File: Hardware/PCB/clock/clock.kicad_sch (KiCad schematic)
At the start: 58 parts, among them J1 AudioJack2, J2 Synth_power_2x5, J3 AudioJack2, J4 AudioJack2, J5 AudioJack2, J6 AudioJack2, J7 AudioJack2, J8 Conn_02x04_Odd_Even, J9 Conn_02x04_Odd_Even, Q1 2N3904, SW1 RotaryEncoder, SW2 SW_Push, U1 40106

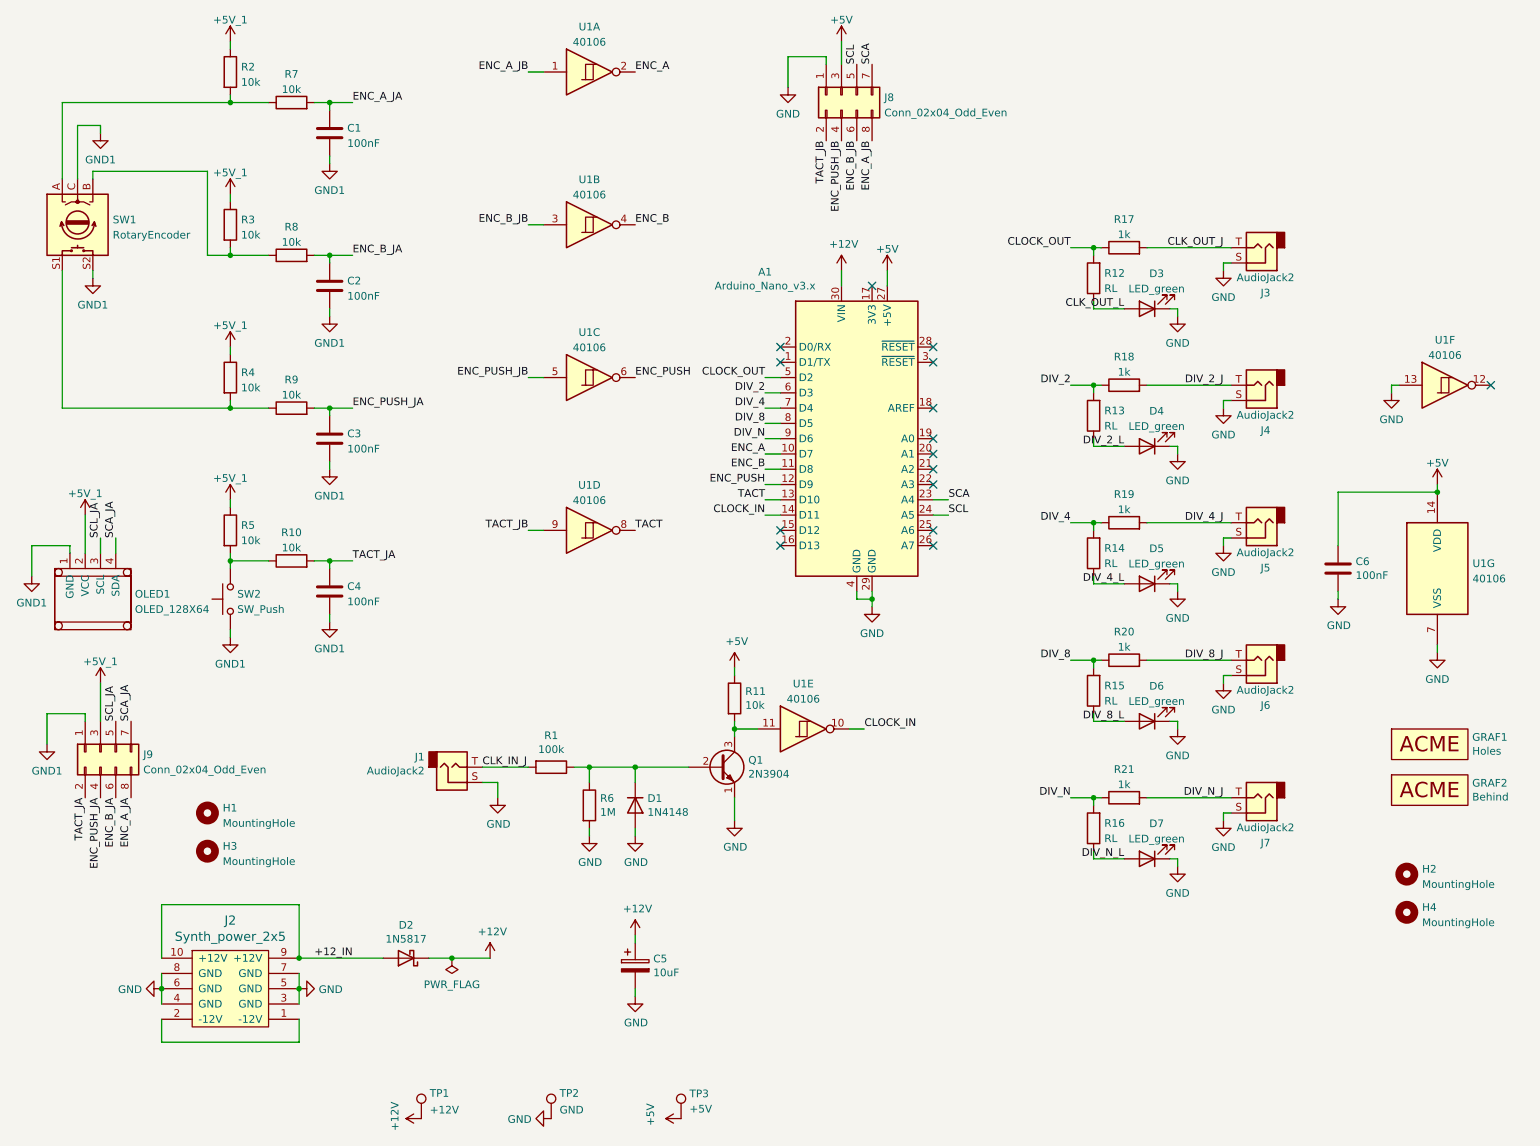
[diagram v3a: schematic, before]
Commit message: Add Zeners, reallocate XORs
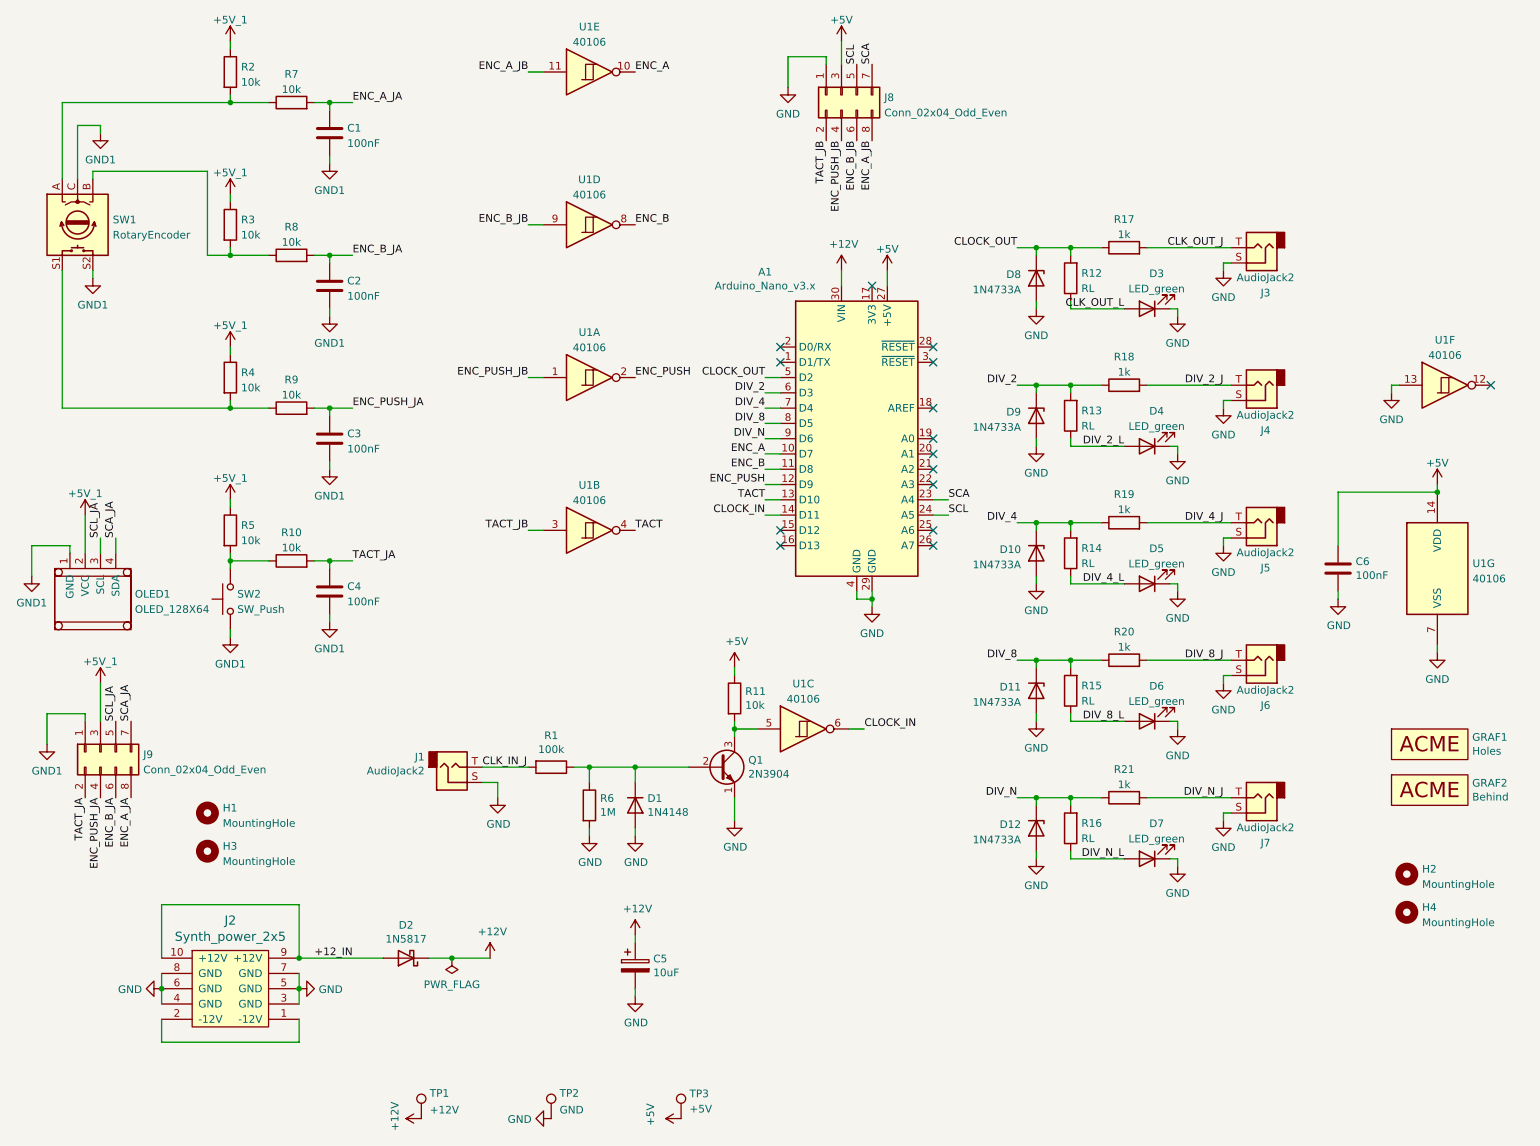
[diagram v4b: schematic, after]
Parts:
- added D10, D11, D12, D8, D9: 1N4733A, ao_tht:D_DO-41_SOD81_P10.16mm_Horizontal, symbol ao_symbols:1N4733A
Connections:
- net CLOCK_IN: now also U1.6; no longer U1.10
- net CLOCK_OUT: now also D8.1 (K)
- net DIV_2: now also D9.1 (K)
- net DIV_4: now also D10.1 (K)
- net DIV_8: now also D11.1 (K)
- net DIV_N: now also D12.1 (K)
- net ENC_A: now also U1.10; no longer U1.2
- net ENC_A_JB: now also U1.11; no longer U1.1
- net ENC_B: now also U1.8; no longer U1.4
- net ENC_B_JB: now also U1.9; no longer U1.3
- net ENC_PUSH: now also U1.2; no longer U1.6
- net ENC_PUSH_JB: now also U1.1; no longer U1.5
- net GND: now also D10.2 (A), D11.2 (A), D12.2 (A), D8.2 (A), D9.2 (A)
- net TACT: now also U1.4; no longer U1.8
- net TACT_JB: now also U1.3; no longer U1.9
- net at Q1.3 (C), R11.2: now also U1.5; no longer U1.11
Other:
- moved on the sheet: R12, R13, R14, R15, R16, U1A, U1B, U1C, U1D, U1E

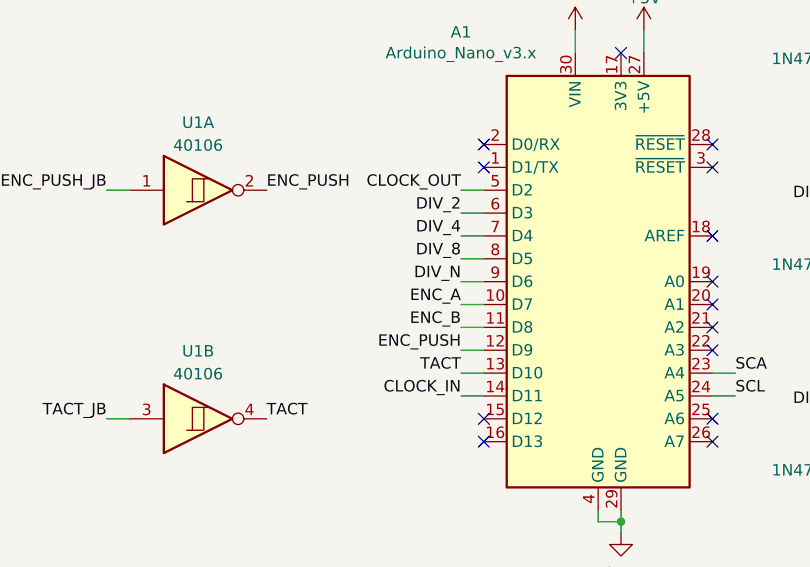
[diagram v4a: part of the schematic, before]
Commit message: Rearrange digital pins (for encoder to interrupt pin 2)
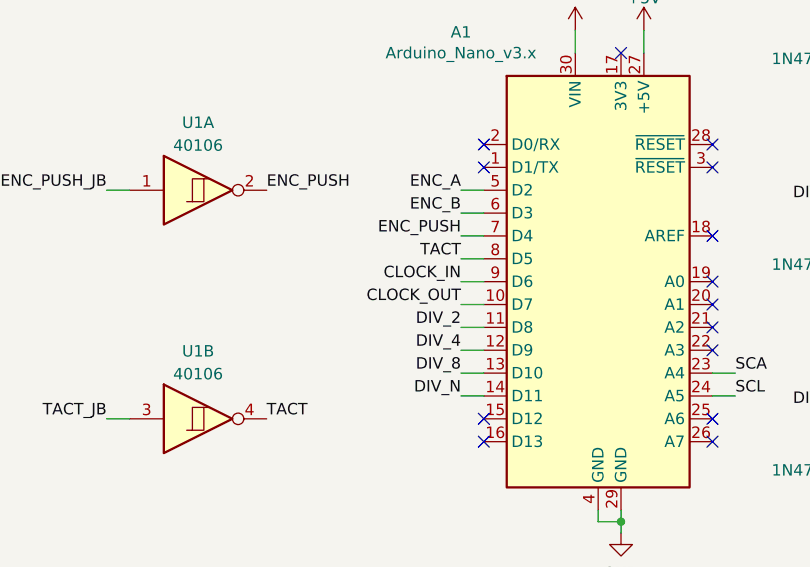
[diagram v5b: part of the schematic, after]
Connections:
- net CLOCK_IN: now also A1.9 (D6); no longer A1.14 (D11)
- net CLOCK_OUT: now also A1.10 (D7); no longer A1.5 (D2)
- net DIV_2: now also A1.11 (D8); no longer A1.6 (D3)
- net DIV_4: now also A1.12 (D9); no longer A1.7 (D4)
- net DIV_8: now also A1.13 (D10); no longer A1.8 (D5)
- net DIV_N: now also A1.14 (D11); no longer A1.9 (D6)
- net ENC_A: now also A1.5 (D2); no longer A1.10 (D7)
- net ENC_B: now also A1.6 (D3); no longer A1.11 (D8)
- net ENC_PUSH: now also A1.7 (D4); no longer A1.12 (D9)
- net TACT: now also A1.8 (D5); no longer A1.13 (D10)
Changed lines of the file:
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@@
     )
   )
-  (label "ENC_A" (at 139.7 88.9 180)
+  (label "ENC_A" (at 139.7 76.2 180)
     (effects (font (size 1.27 1.27)) (justify right bottom))
   )
@@
     (effects (font (size 1.27 1.27)) (justify left bottom))
   )
-  (label "DIV_N" (at 139.7 86.36 180)
+  (label "DIV_N" (at 139.7 99.06 180)
     (effects (font (size 1.27 1.27)) (justify right bottom))
   )
@@
     (effects (font (size 1.27 1.27)) (justify right bottom))
   )
-  (label "CLOCK_OUT" (at 139.7 76.2 180)
+  (label "CLOCK_OUT" (at 139.7 88.9 180)
     (effects (font (size 1.27 1.27)) (justify right bottom))
   )
@@
     (effects (font (size 1.27 1.27)) (justify left bottom))
   )
-  (label "DIV_2" (at 139.7 78.74 180)
+  (label "DIV_2" (at 139.7 91.44 180)
     (effects (font (size 1.27 1.27)) (justify right bottom))
   )
@@
     (effects (font (size 1.27 1.27)) (justify right bottom))
   )
-  (label "TACT" (at 139.7 96.52 180)
+  (label "TACT" (at 139.7 83.82 180)
     (effects (font (size 1.27 1.27)) (justify right bottom))
   )
@@
     (effects (font (size 1.27 1.27)) (justify left bottom))
   )
-  (label "CLOCK_IN" (at 139.7 99.06 180)
+  (label "CLOCK_IN" (at 139.7 86.36 180)
     (effects (font (size 1.27 1.27)) (justify right bottom))
   )
@@
     (effects (font (size 1.27 1.27)) (justify right bottom))
   )
-  (label "ENC_B" (at 139.7 91.44 180)
+  (label "ENC_B" (at 139.7 78.74 180)
     (effects (font (size 1.27 1.27)) (justify right bottom))
   )
-  (label "ENC_PUSH" (at 139.7 93.98 180)
+  (label "ENC_PUSH" (at 139.7 81.28 180)
     (effects (font (size 1.27 1.27)) (justify right bottom))
   )
@@
     (effects (font (size 1.27 1.27)) (justify right bottom))
   )
-  (label "DIV_4" (at 139.7 81.28 180)
+  (label "DIV_4" (at 139.7 93.98 180)
     (effects (font (size 1.27 1.27)) (justify right bottom))
   )
@@
     (effects (font (size 1.27 1.27)) (justify right bottom))
   )
-  (label "DIV_8" (at 139.7 83.82 180)
+  (label "DIV_8" (at 139.7 96.52 180)
     (effects (font (size 1.27 1.27)) (justify right bottom))
   )

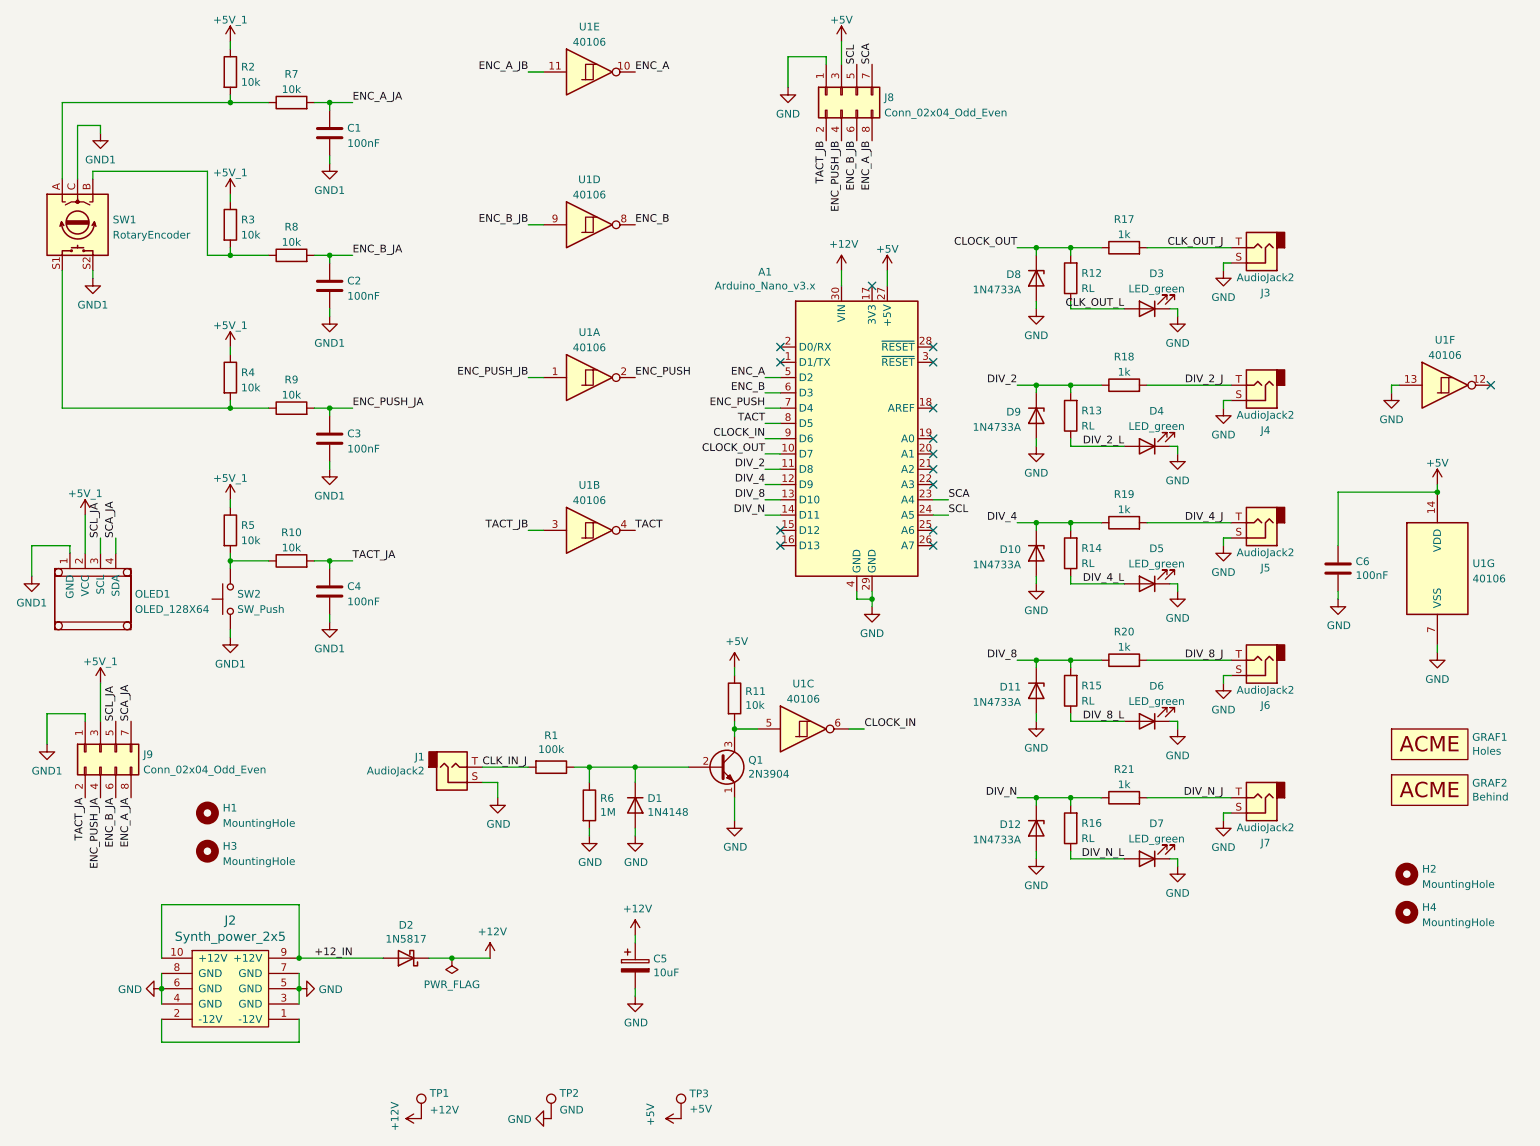
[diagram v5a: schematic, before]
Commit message: rm external clock, add beat output
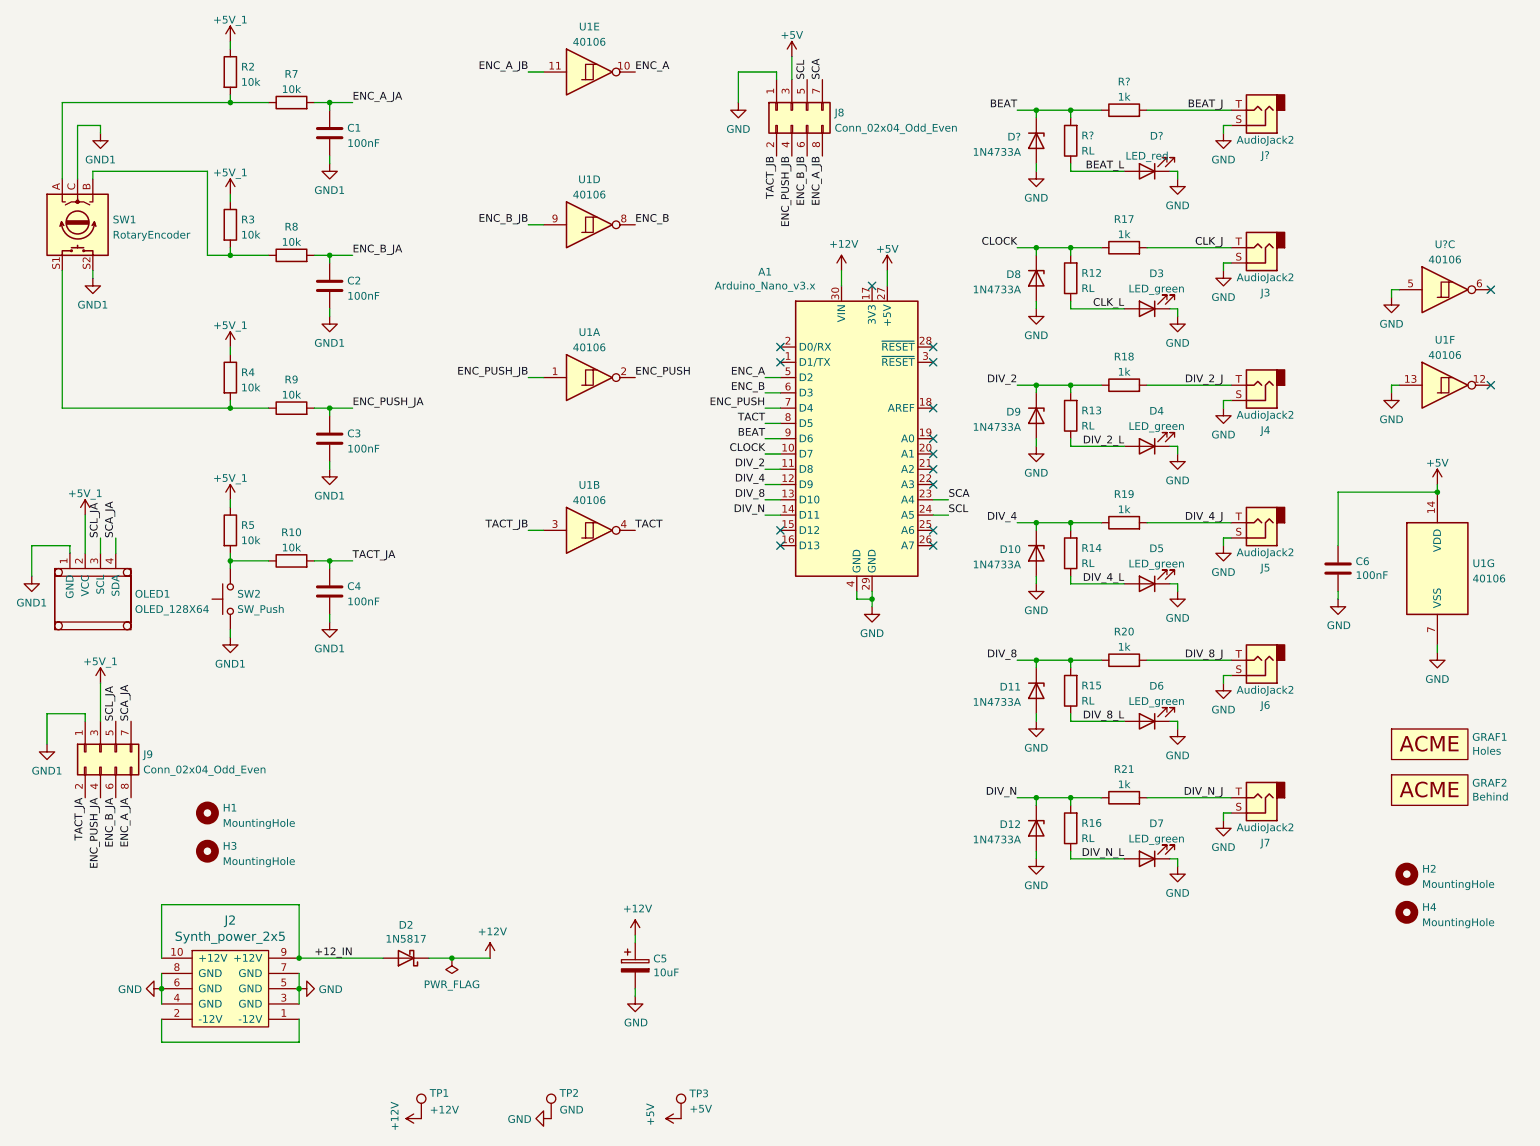
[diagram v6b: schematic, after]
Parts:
- removed D1: 1N4148, ao_tht:D_DO-35_SOD27_P7.62mm_Horizontal, symbol ao_symbols:1N4148
- removed J1: AudioJack2, ao_tht:Jack_6.35mm_PJ_629HAN_slots, symbol ao_symbols:AudioJack2
- removed Q1: 2N3904, ao_tht:TO-92_Inline_Wide, symbol ao_symbols:2N3904
- removed R1: 100k, ao_tht:R_Axial_DIN0204_L3.6mm_D1.6mm_P7.62mm_Horizontal, symbol ao_symbols:R
- removed R11: 10k, ao_tht:R_Axial_DIN0204_L3.6mm_D1.6mm_P7.62mm_Horizontal, symbol ao_symbols:R
- removed R6: 1M, ao_tht:R_Axial_DIN0204_L3.6mm_D1.6mm_P7.62mm_Horizontal, symbol ao_symbols:R
- removed unit 3 of U1
- added D?: 1N4733A, ao_tht:D_DO-41_SOD81_P10.16mm_Horizontal, symbol ao_symbols:1N4733A
- added D?: LED_red, ao_tht:LED_D5.0mm, symbol ao_symbols:LED_red
- added J?: AudioJack2, ao_tht:Jack_6.35mm_PJ_629HAN_slots, symbol ao_symbols:AudioJack2
- added R?: 1k, ao_tht:R_Axial_DIN0204_L3.6mm_D1.6mm_P7.62mm_Horizontal, symbol ao_symbols:R
- added R?: RL, ao_tht:R_Axial_DIN0204_L3.6mm_D1.6mm_P7.62mm_Horizontal, symbol ao_symbols:R
- added U?: 40106, ao_tht:DIP-14_W7.62mm_Socket_LongPads, symbol 4xxx:40106
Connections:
- net GND: now also D?.1 (K), D?.2 (A), J?.S, U?.5
- net CLK_OUT_J renamed CLK_J
- net CLK_OUT_L renamed CLK_L
- net CLOCK_IN renamed BEAT
- net BEAT: now also D?.1 (K), R?.1, R?.2
- net CLOCK_OUT renamed CLOCK
- new net BEAT_J: J?.T, R?.2
- new net BEAT_L: D?.2 (A), R?.1
- no-connect marks 15 -> 16
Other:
- moved on the sheet: J8
